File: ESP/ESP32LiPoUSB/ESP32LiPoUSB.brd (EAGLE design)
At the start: 50.8 x 34.5 mm, 29 parts, among them Q1 mmbt2222, Q2 mmbt2222, Q3 DMG3415U, SW2 KMR2, X1 JSTPH, X2 ESP32_WROOM32_SKINNY

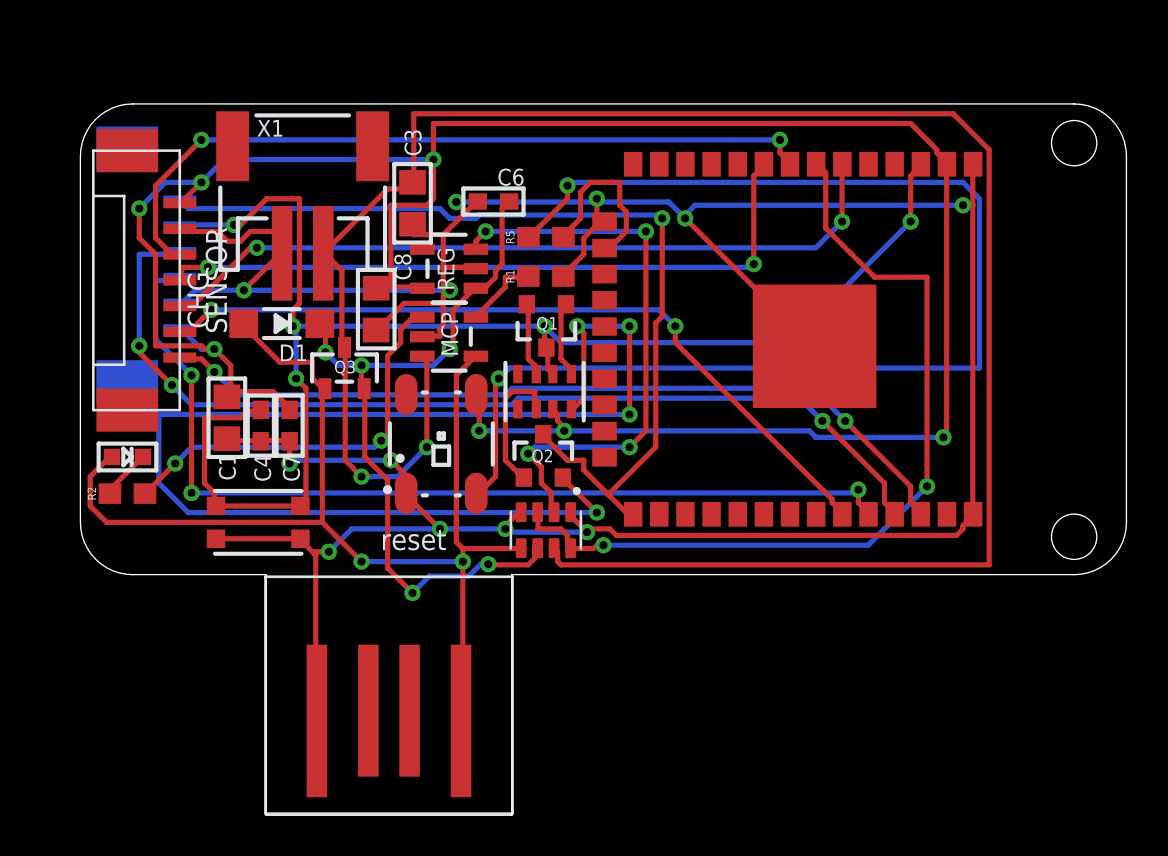
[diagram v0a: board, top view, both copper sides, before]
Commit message: take out autoprgm
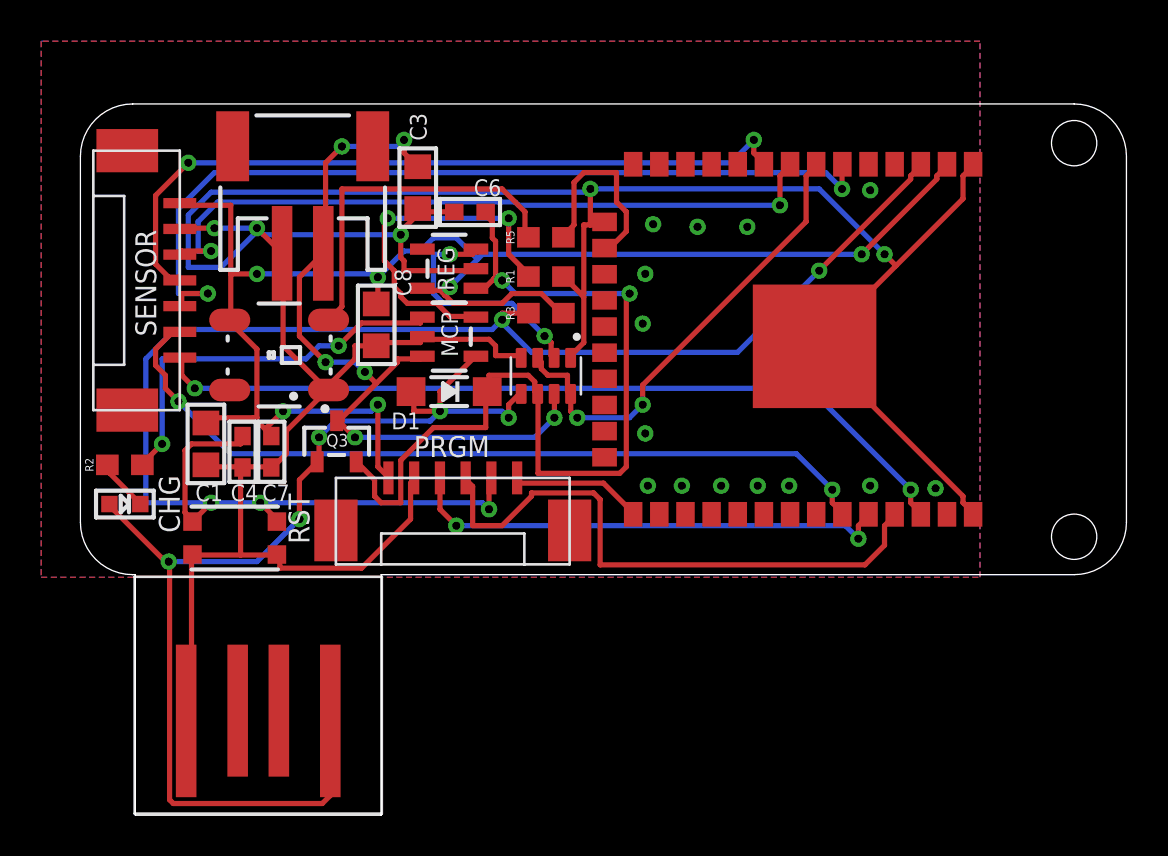
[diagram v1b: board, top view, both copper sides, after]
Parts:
- removed PROGRAMMER: JST_1.25_6P, Scott-Connectors:JST1.25_6P
- removed Q1, Q2: mmbt2222, SparkFun:SOT23-3
- removed R13: 10K, microbuilder:RESPACK_4X0603
- removed U$13: (no value), microbuilder:PCBFEAT-REV-040
- removed U$43: (no value), silks:HUZZAH32
- removed U$7: (no value), microbuilder:ADAFRUIT_5MM
- removed U$9: (no value), silks:FEATHERLOGO_MED
- added PRGM: JST_1.25_6P, Scott-Connectors:JST1.25_6P
- added R3: 10K, Scott-Electrical:0603
- moved RGB 8.98 mm to (9.65, 10.7), turned to 180 degrees
- moved D1 8.77 mm to (17.9, 8.89)
- moved RA1 7.49 mm to (22.6, 9.65)
- moved U$12 6.35 mm to (8.64, -6.60)
- moved Q3 3.58 mm to (12.4, 6.48)
- moved CHG 2.29 mm to (2.16, 3.43)
- moved C1 1.63 mm to (6.10, 6.35)
- moved C4 1.55 mm to (7.87, 5.97)
- moved C7 1.55 mm to (9.27, 5.97)
- moved R2 1.40 mm to (2.16, 5.33)
- moved SW2 1.37 mm to (7.49, 1.78)
- moved C6 1.25 mm to (18.9, 17.6)
- moved C3 0.80 mm to (16.4, 18.8)
- moved C8 0.76 mm to (14.4, 12.1)
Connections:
- removed net DTR: Q2.2, R13.4
- removed net N$12: Q1.1, R13.5
- removed net N$13: Q2.1, R13.2
- removed net RTS: Q1.2, R13.7
- net 3.3V: now also PRGM.6, R3.2; no longer PROGRAMMER.6, R13.3
- net GND: now also PRGM.5; no longer PROGRAMMER.5
- net GPIO0: now also PRGM.1; no longer PROGRAMMER.1, Q2.3
- net RESET: now also PRGM.2, R3.1; no longer PROGRAMMER.2, Q1.3, R13.6
- net RXD0: now also PRGM.4; no longer PROGRAMMER.4
- net TXD0: now also PRGM.3; no longer PROGRAMMER.3
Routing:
- net VBAT: track 99.8 -> 37.6 mm, vias 2 -> 6
- net DTR: track 61.7 -> 0.00 mm, vias 4 -> 0
- net N$2: track 61.6 -> 17.3 mm, vias 2 -> 0
- net GPIO0: track 44.7 -> 6.51 mm, vias 1 -> 0
- net 3.3V: track 112.3 -> 77.1 mm, vias 7 -> 6
- net RXD0: track 46.1 -> 23.8 mm, vias 3 -> 2
- net TXD0: track 47.6 -> 28.6 mm, vias 3 -> 0
- net A13_I35: track 41.0 -> 22.9 mm
- net EN: track 28.1 -> 11.7 mm, vias 4 -> 2
- net N$4: track 3.67 -> 17.3 mm, vias 0 -> 2
- net N$7: track 36.2 -> 44.2 mm, vias 5 -> 2
- net RESET: track 71.4 -> 79.4 mm
- net N$13: track 6.70 -> 0.00 mm
- net A2_I34: track 36.7 -> 41.9 mm
- net GND: track 158.5 -> 153.5 mm, vias 12 -> 19
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- added copper zone on layer 1, net GND
- added copper zone on layer 16, net GND
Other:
- outline, holes or cut-outs redrawn
- board text added: "ESP32 LiPo V1"
- board text added: "May 12, 2019"
- board text removed: "12/A11"
- board text removed: "13/A12"
- board text removed: "14/A6"
- board text removed: "15/A8"
- board text removed: "21"
- board text removed: "27/A10"
- board text removed: "3.7/4.2V LiPoly Batt µUSB charge"
- board text removed: "32/A7"
- board text removed: "33/A9"
- board text removed: "3V"
- board text removed: "A0 DAC2"
- board text removed: "A1 DAC1"
- board text removed: "A2/34"
- board text removed: "A3/39"
- board text removed: "A4/36"
- board text removed: "A5/4"
- board text removed: "BAT"
- board text removed: "Contains FCCID 2AC7Z-ESP32"
- board text removed: "ESP32 Feather 16MB Flash WiFI+BT"
- board text removed: "En"
- board text removed: "GND"
- board text removed: "MISO/19"
- board text removed: "MOSI/18"
- board text removed: "NC"
- board text removed: "RX/16"
- board text removed: "SCK/5"
- board text removed: "SCL/22"
- board text removed: "SDA/23"
- board text removed: "TX/17"
- board text removed: "USB"
- board text removed: "reset"
